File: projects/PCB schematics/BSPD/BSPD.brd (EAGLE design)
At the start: 99.1 x 99.1 mm, 83 parts, among them X1 5566-2, X2 5566-2, X3 5566-4

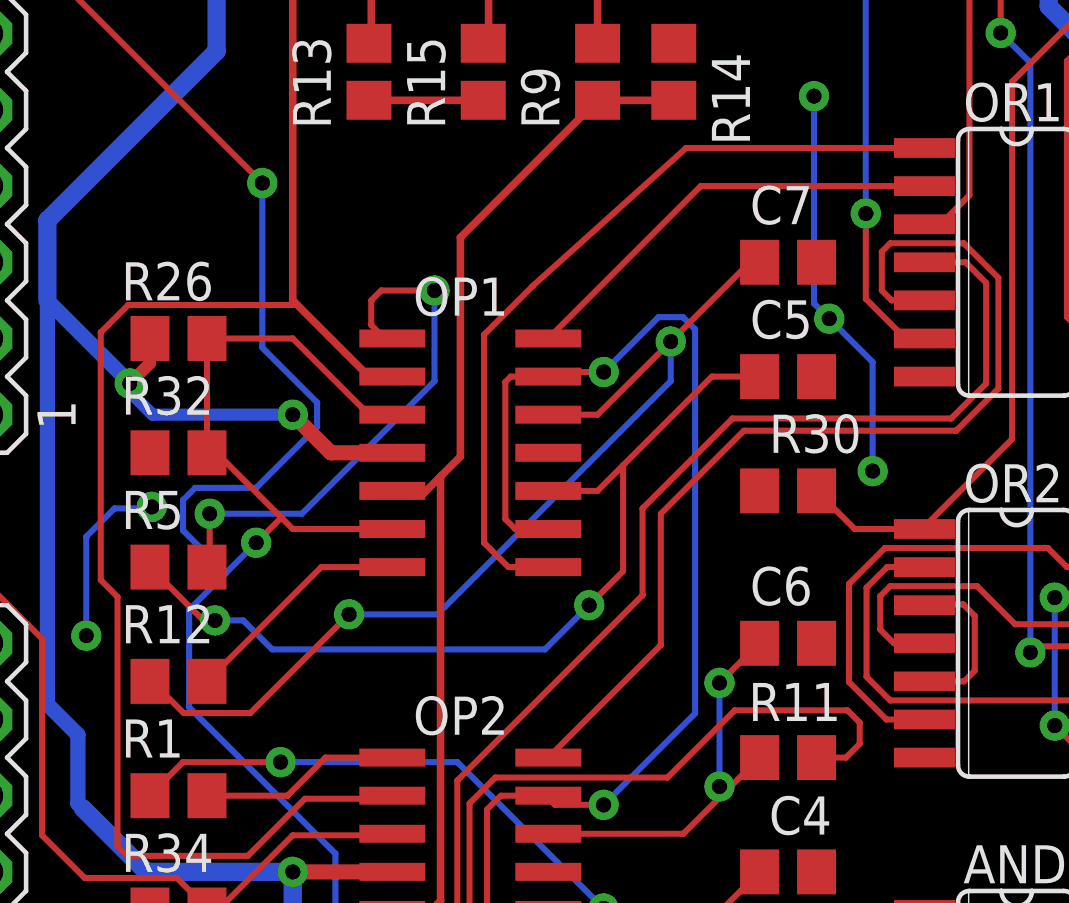
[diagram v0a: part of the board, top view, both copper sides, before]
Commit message: BSPD - Minor changes
Small clearance changes.
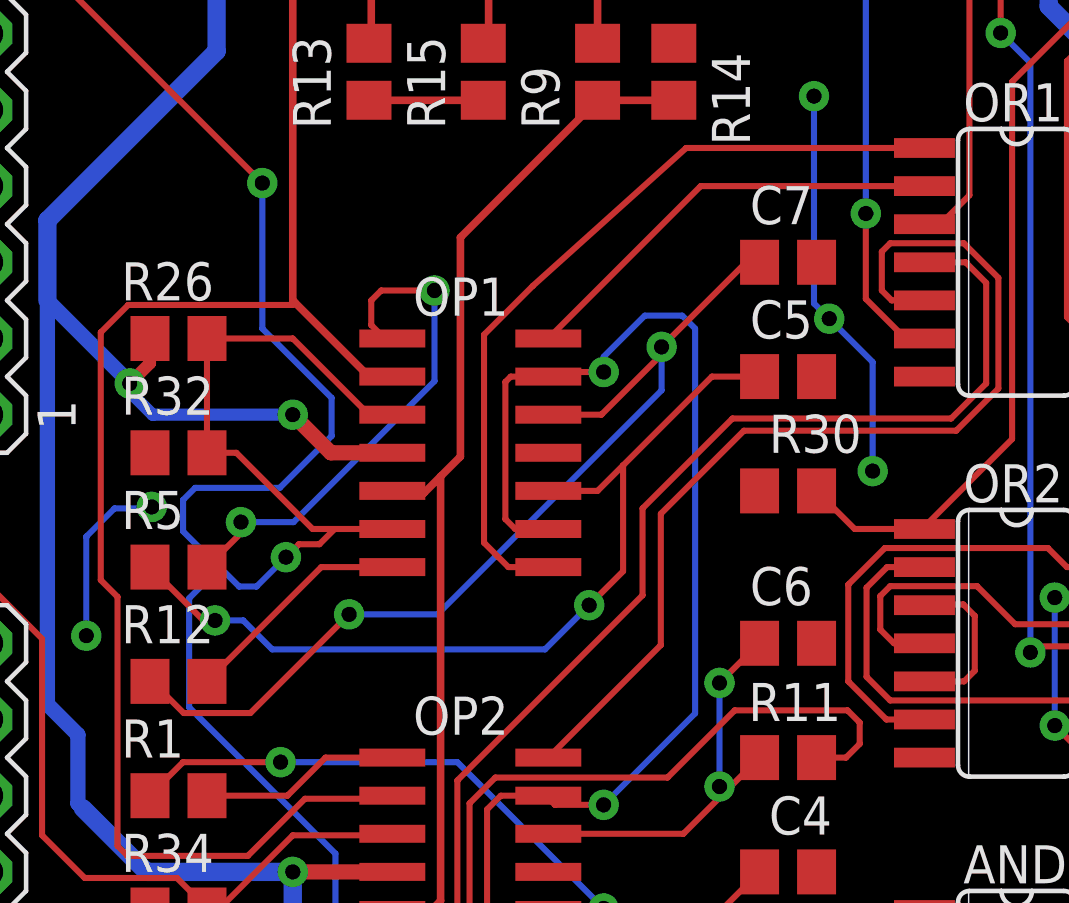
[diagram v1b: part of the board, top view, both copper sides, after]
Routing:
- net BSE_PROCESSED: track 94.3 -> 97.2 mm
- net N$7: track 18.1 -> 17.3 mm
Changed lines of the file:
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@@
 <wire x1="40.64" y1="58.42" x2="43.18" y2="55.88" width="0.2032" layer="1"/>
 <wire x1="43.18" y1="55.88" x2="43.9582" y2="55.88" width="0.2032" layer="1"/>
-<wire x1="43.9582" y1="52.07" x2="40.64" y2="52.07" width="0.2032" layer="1"/>
-<wire x1="40.64" y1="52.07" x2="40.259" y2="52.451" width="0.2032" layer="1"/>
-<wire x1="40.259" y1="52.451" x2="38.1" y2="54.61" width="0.2032" layer="1"/>
-<wire x1="38.1" y1="54.61" x2="37.78" y2="54.61" width="0.2032" layer="1"/>
+<wire x1="43.9582" y1="52.07" x2="42.037" y2="52.07" width="0.2032" layer="1"/>
+<wire x1="42.037" y1="52.07" x2="41.3004" y2="52.07" width="0.2032" layer="1"/>
+<wire x1="40.8432" y1="51.562" x2="41.529" y2="51.562" width="0.2032" layer="1"/>
+<wire x1="41.3004" y1="52.07" x2="38.7604" y2="54.61" width="0.2032" layer="1"/>
+<wire x1="38.7604" y1="54.61" x2="37.78" y2="54.61" width="0.2032" layer="1"/>
 <wire x1="43.2816" y1="30.48" x2="43.9582" y2="30.48" width="0.2032" layer="1"/>
 <wire x1="42.0624" y1="31.6992" x2="43.2816" y2="30.48" width="0.2032" layer="1"/>
 <wire x1="42.0624" y1="41.2496" x2="42.0624" y2="31.6992" width="0.2032" layer="16"/>
 <wire x1="37.1856" y1="46.1264" x2="42.0624" y2="41.2496" width="0.2032" layer="16"/>
-<wire x1="37.1856" y1="49.3776" x2="37.1856" y2="46.1264" width="0.2032" layer="16"/>
-<wire x1="39.4208" y1="51.6128" x2="38.4048" y2="50.5968" width="0.2032" layer="16"/>
-<wire x1="38.4048" y1="50.5968" x2="37.1856" y2="49.3776" width="0.2032" layer="16"/>
-<wire x1="40.259" y1="52.451" x2="39.4208" y2="51.6128" width="0.2032" layer="1"/>
+<wire x1="37.1856" y1="49.7586" x2="37.1856" y2="46.1264" width="0.2032" layer="16"/>
+<wire x1="40.4114" y1="51.1302" x2="39.4335" y2="50.1523" width="0.2032" layer="16"/>
+<wire x1="39.4335" y1="50.1523" x2="38.8493" y2="50.1523" width="0.2032" layer="16"/>
+<wire x1="38.2143" y1="50.7873" x2="38.2016" y2="50.7746" width="0.2032" layer="16"/>
+<wire x1="38.2016" y1="50.7746" x2="37.1856" y2="49.7586" width="0.2032" layer="16"/>
+<wire x1="40.8432" y1="51.562" x2="40.4114" y2="51.1302" width="0.2032" layer="1"/>
 <wire x1="20.9296" y1="82.296" x2="15.24" y2="82.296" width="0.2032" layer="1"/>
 <wire x1="39.624" y1="63.6016" x2="20.9296" y2="82.296" width="0.2032" layer="1"/>
-<wire x1="39.624" y1="58.1152" x2="39.624" y2="63.6016" width="0.2032" layer="16"/>
-<wire x1="41.4528" y1="56.2864" x2="39.624" y2="58.1152" width="0.2032" layer="16"/>
-<wire x1="41.4528" y1="55.4736" x2="41.4528" y2="56.2864" width="0.2032" layer="16"/>
-<wire x1="39.4208" y1="53.4416" x2="41.4528" y2="55.4736" width="0.2032" layer="16"/>
-<wire x1="37.3888" y1="53.4416" x2="39.4208" y2="53.4416" width="0.2032" layer="16"/>
+<wire x1="39.624" y1="58.7502" x2="39.624" y2="63.6016" width="0.2032" layer="16"/>
+<wire x1="41.9354" y1="56.4388" x2="39.624" y2="58.7502" width="0.2032" layer="16"/>
+<wire x1="41.9354" y1="55.1688" x2="41.9354" y2="56.4388" width="0.2032" layer="16"/>
+<wire x1="40.2082" y1="53.4416" x2="41.9354" y2="55.1688" width="0.2032" layer="16"/>
+<wire x1="37.3888" y1="53.4416" x2="40.2082" y2="53.4416" width="0.2032" layer="16"/>
 <wire x1="36.9824" y1="53.0352" x2="37.3888" y2="53.4416" width="0.2032" layer="16"/>
-<wire x1="36.9824" y1="52.0192" x2="36.9824" y2="53.0352" width="0.2032" layer="16"/>
-<wire x1="38.4048" y1="50.5968" x2="36.9824" y2="52.0192" width="0.2032" layer="16"/>
+<wire x1="36.9824" y1="51.9938" x2="36.9824" y2="53.0352" width="0.2032" layer="16"/>
+<wire x1="38.8493" y1="50.1523" x2="38.2143" y2="50.7873" width="0.2032" layer="16"/>
+<wire x1="38.2016" y1="50.7746" x2="36.9824" y2="51.9938" width="0.2032" layer="16"/>
 <wire x1="15.24" y1="82.296" x2="15.24" y2="82.34" width="0.2032" layer="1"/>
 <via x="42.0624" y="31.6992" extent="1-16" drill="0.508"/>
-<via x="39.4208" y="51.6128" extent="1-16" drill="0.508"/>
+<via x="40.4114" y="51.1302" extent="1-16" drill="0.508"/>
 <via x="39.624" y="63.6016" extent="1-16" drill="0.508"/>
+<wire x1="41.529" y1="51.562" x2="42.037" y2="52.07" width="0.2032" layer="1"/>
 </signal>
 <signal name="MOTCUR_PROCESSED">
@@
 <contactref element="OP1" pad="1"/>
 <contactref element="R5" pad="1"/>
-<wire x1="37.78" y1="50.8" x2="37.8714" y2="50.8914" width="0.2032" layer="1"/>
-<wire x1="37.8714" y1="50.8914" x2="37.8714" y2="52.578" width="0.2032" layer="1"/>
-<via x="37.8714" y="52.578" extent="1-16" drill="0.508"/>
-<wire x1="37.8714" y1="52.578" x2="40.9448" y2="52.578" width="0.2032" layer="16"/>
+<wire x1="37.78" y1="50.8" x2="38.9128" y2="51.9328" width="0.2032" layer="1"/>
+<wire x1="38.9128" y1="51.9328" x2="38.9128" y2="52.2986" width="0.2032" layer="1"/>
+<via x="38.9128" y="52.2986" extent="1-16" drill="0.508"/>
+<wire x1="38.9128" y1="52.2986" x2="40.6654" y2="52.2986" width="0.2032" layer="16"/>
 <wire x1="45.3644" y1="56.9976" x2="45.3644" y2="60.0202" width="0.2032" layer="16"/>
 <via x="45.3644" y="60.0202" extent="1-16" drill="0.508"/>
@@
 <wire x1="43.7042" y1="58.42" x2="43.9582" y2="58.42" width="0.2032" layer="1"/>
 <wire x1="43.7042" y1="58.42" x2="43.2562" y2="58.868" width="0.2032" layer="1"/>
-<wire x1="40.9448" y1="52.578" x2="45.3644" y2="56.9976" width="0.2032" layer="16"/>
+<wire x1="40.6654" y1="52.2986" x2="45.3644" y2="56.9976" width="0.2032" layer="16"/>
 <wire x1="43.5864" y1="60.0202" x2="43.2562" y2="59.69" width="0.2032" layer="1"/>
 <wire x1="43.2562" y1="59.69" x2="43.2562" y2="58.868" width="0.2032" layer="1"/>
@@
 <contactref element="C7" pad="1"/>
 <contactref element="OP1" pad="12"/>
-<wire x1="49.1582" y1="55.88" x2="50.8" y2="55.88" width="0.2032" layer="1"/>
-<wire x1="50.8" y1="55.88" x2="53.2384" y2="58.3184" width="0.2032" layer="1"/>
-<wire x1="53.2384" y1="58.3184" x2="55.88" y2="60.96" width="0.2032" layer="1"/>
-<wire x1="55.88" y1="60.96" x2="56.2" y2="60.96" width="0.2032" layer="1"/>
+<wire x1="49.1582" y1="55.88" x2="50.927" y2="55.88" width="0.2032" layer="1"/>
+<wire x1="52.9336" y1="57.8866" x2="52.9336" y2="58.1406" width="0.2032" layer="1"/>
+<wire x1="52.9336" y1="57.8866" x2="50.927" y2="55.88" width="0.2032" layer="1"/>
+<wire x1="52.9336" y1="58.1406" x2="55.753" y2="60.96" width="0.2032" layer="1"/>
+<wire x1="55.753" y1="60.96" x2="56.2" y2="60.96" width="0.2032" layer="1"/>
 <via x="42.5176125" y="49.2252" extent="1-16" drill="0.508"/>
 <wire x1="35.88" y1="46.99" x2="35.94895" y2="46.99" width="0.2032" layer="1"/>
@@
 <wire x1="39.2276125" y1="45.9352" x2="42.5176125" y2="49.2252" width="0.2032" layer="1"/>
 <wire x1="42.5176125" y1="49.2252" x2="45.466" y2="49.2252" width="0.2032" layer="16"/>
-<wire x1="45.466" y1="49.2252" x2="53.2384" y2="56.9976" width="0.2032" layer="16"/>
-<wire x1="53.2384" y1="56.9976" x2="53.2384" y2="58.3184" width="0.2032" layer="16"/>
-<via x="53.2384" y="58.3184" extent="1-16" drill="0.508"/>
+<wire x1="45.466" y1="49.2252" x2="52.9336" y2="56.6928" width="0.2032" layer="16"/>
+<wire x1="52.9336" y1="56.6928" x2="52.9336" y2="58.1406" width="0.2032" layer="16"/>
+<via x="52.9336" y="58.1406" extent="1-16" drill="0.508"/>
 </signal>
 <signal name="TIME_THRESH">
@@
 <wire x1="56.2864" y1="33.7312" x2="56.2" y2="33.02" width="0.2032" layer="1"/>
 <wire x1="51.0032" y1="57.3024" x2="49.1744" y2="57.3024" width="0.2032" layer="1"/>
-<wire x1="52.832" y1="59.1312" x2="51.0032" y2="57.3024" width="0.2032" layer="16"/>
-<wire x1="53.6448" y1="59.1312" x2="52.832" y2="59.1312" width="0.2032" layer="16"/>
-<wire x1="54.0512" y1="58.7248" x2="53.6448" y2="59.1312" width="0.2032" layer="16"/>
-<wire x1="54.0512" y1="45.9232" x2="54.0512" y2="58.7248" width="0.2032" layer="16"/>
+<wire x1="52.3748" y1="59.182" x2="51.0032" y2="57.8104" width="0.2032" layer="16"/>
+<wire x1="51.0032" y1="57.8104" x2="51.0032" y2="57.3024" width="0.2032" layer="16"/>
+<wire x1="53.6194" y1="59.182" x2="52.3748" y2="59.182" width="0.2032" layer="16"/>
+<wire x1="54.0512" y1="58.7502" x2="53.6194" y2="59.182" width="0.2032" layer="16"/>
+<wire x1="54.0512" y1="45.9232" x2="54.0512" y2="58.7502" width="0.2032" layer="16"/>
 <wire x1="51.0032" y1="42.8752" x2="54.0512" y2="45.9232" width="0.2032" layer="16"/>
 <wire x1="49.3776" y1="42.8752" x2="51.0032" y2="42.8752" width="0.2032" layer="1"/>
@@
 <contactref element="OR2" pad="13"/>
 <wire x1="61.6966" y1="45.72" x2="60.42735" y2="45.72" width="0.2032" layer="1"/>
-<wire x1="60.42735" y1="45.72" x2="59.182" y2="46.96535" width="0.2032" layer="1"/>
-<wire x1="59.182" y1="46.96535" x2="59.182" y2="50.2412" width="0.2032" layer="1"/>
-<wire x1="59.182" y1="50.2412" x2="60.3758" y2="51.435" width="0.2032" layer="1"/>
+<wire x1="60.42735" y1="45.72" x2="59.1566" y2="46.99075" width="0.2032" layer="1"/>
+<wire x1="59.1566" y1="46.99075" x2="59.1566" y2="50.2158" width="0.2032" layer="1"/>
+<wire x1="59.1566" y1="50.2158" x2="60.3758" y2="51.435" width="0.2032" layer="1"/>
 <wire x1="60.3758" y1="51.435" x2="65.81065" y2="51.435" width="0.2032" layer="1"/>
 <wire x1="66.44565" y1="50.8" x2="67.8434" y2="50.8" width="0.2032" layer="1"/>
